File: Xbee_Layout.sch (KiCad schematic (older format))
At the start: 7 parts

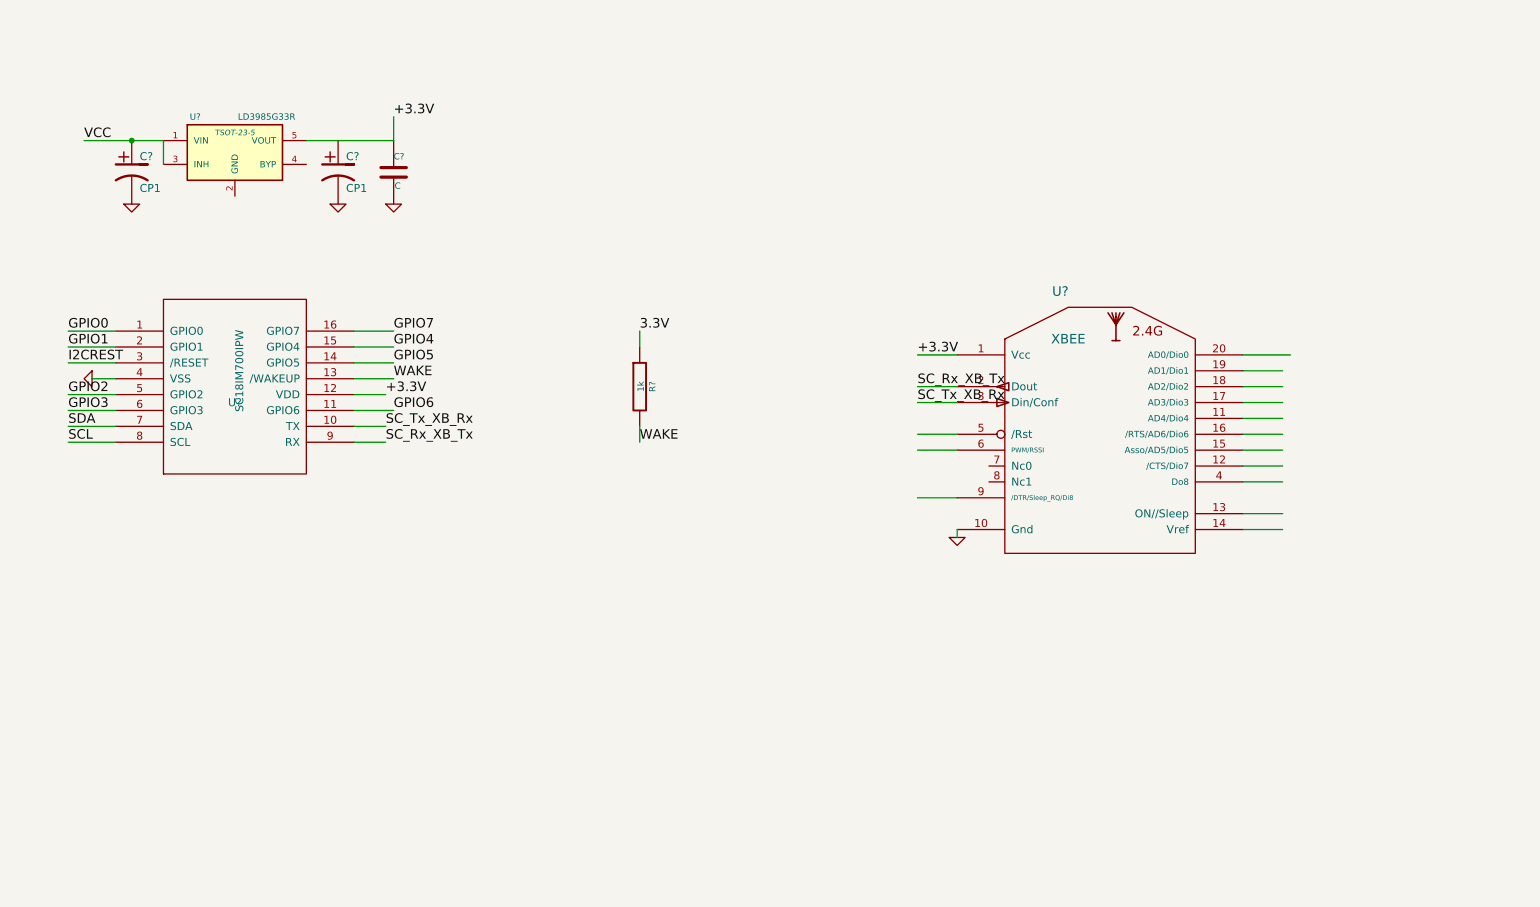
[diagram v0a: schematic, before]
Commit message: Added connectors and Jumpers
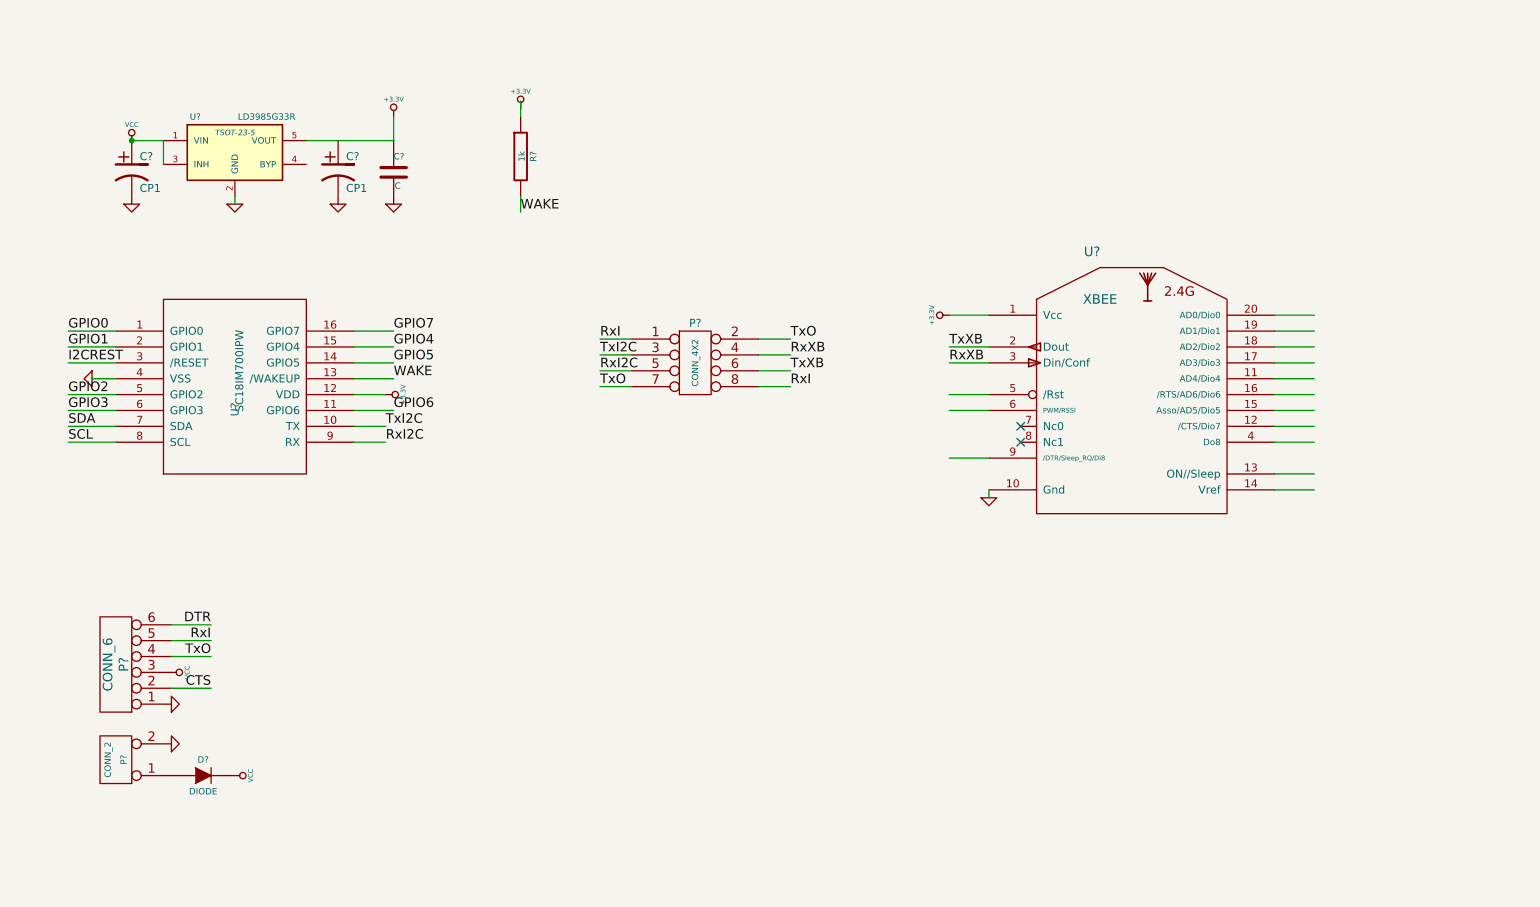
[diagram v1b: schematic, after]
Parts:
- added D?: DIODE, ~, symbol DIODE
- added P?: CONN_4X2, symbol CONN_4X2
- added P?: CONN_6, symbol CONN_6
- added P?: CONN_2, symbol CONN_2
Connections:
- net labels added: CTS, DTR, RxI, RxI2C, RxXB, TxI2C, TxO, TxXB
- net labels removed: 3.3V, SC_Rx_XB_Tx, SC_Tx_XB_Rx
- wire segments 40 -> 53
- no-connect marks 0 -> 2
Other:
- moved on the sheet: R?, U?

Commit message: I  dont kow
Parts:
- removed U?: SC18IM700IPW, TSSOP16, symbol SC18IM700IPW
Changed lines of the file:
@@
 LIBS:contrib
 LIBS:valves
+LIBS:SC18700IPW
 LIBS:Xbee_Layout-cache
 EELAYER 27 0
@@
 Sheet 1 1
 Title "noname.sch"
-Date "11 aug 2014"
+Date "12 aug 2014"
 Rev ""
 Comp ""
@@
 $EndDescr
 $Comp
-L SC18IM700IPW U?
-U 1 1 53E71C01
-P 2500 3150
-F 0 "U?" V 2500 3050 50  0000 R CNN
-F 1 "SC18IM700IPW" V 2500 3250 50  0000 C TNN
-F 2 "TSSOP16" H 2500 3150 50  0001 C CNN
-F 3 "DOCUMENTATION" H 2500 3150 50  0001 C CNN
-	1    2500 3150
-	1    0    0    -1
-$EndComp
-$Comp
 L XBEE U?

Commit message: Fixing lib still
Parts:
- removed U?: XBEE, symbol XBEE
- added U?: XBEE, symbol XBEE
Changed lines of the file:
@@
 LIBS:contrib
 LIBS:valves
-LIBS:SC18700IPW
+LIBS:sc18im700ipw
+LIBS:modules_droids
 LIBS:Xbee_Layout-cache
 EELAYER 27 0
@@
 Comment4 ""
 $EndDescr
-$Comp
-L XBEE U?
-U 1 1 53E7200D
-P 8150 3400
-F 0 "U?" H 7900 4500 60  0000 C CNN
-F 1 "XBEE" H 7950 4200 60  0000 C CNN
-F 2 "" H 8150 3400 60  0000 C CNN
-F 3 "" H 8150 3400 60  0000 C CNN
-	1    8150 3400
-	1    0    0    -1
-$EndComp
 $Comp
 L GND #PWR?
@@
 	1    0    0    -1
 $EndComp
+$Comp
+L XBEE U?
+U 1 1 53EA5E0D
+P 8150 3400
+F 0 "U?" H 7900 4500 60  0000 C CNN
+F 1 "XBEE" H 7950 4200 60  0000 C CNN
+F 2 "" H 8150 3400 60  0000 C CNN
+F 3 "" H 8150 3400 60  0000 C CNN
+	1    8150 3400
+	1    0    0    -1
+$EndComp

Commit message: Fixed everything i hope
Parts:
- added U?: SC18IM700IPW, TSSOP-16, symbol SC18IM700IPW
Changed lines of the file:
@@
 LIBS:contrib
 LIBS:valves
-LIBS:sc18im700ipw
 LIBS:modules_droids
 LIBS:Xbee_Layout-cache
@@
 	1    0    0    -1
 $EndComp
+$Comp
+L SC18IM700IPW U?
+U 1 1 53EA6645
+P 2500 3150
+F 0 "U?" H 2150 3750 50  0000 C CNN
+F 1 "SC18IM700IPW" H 2500 3600 50  0000 C CNN
+F 2 "TSSOP-16" H 2750 2550 50  0001 C CNN
+F 3 "DOCUMENTATION" V 2500 3150 50  0001 C CNN
+	1    2500 3150
+	1    0    0    -1
+$EndComp

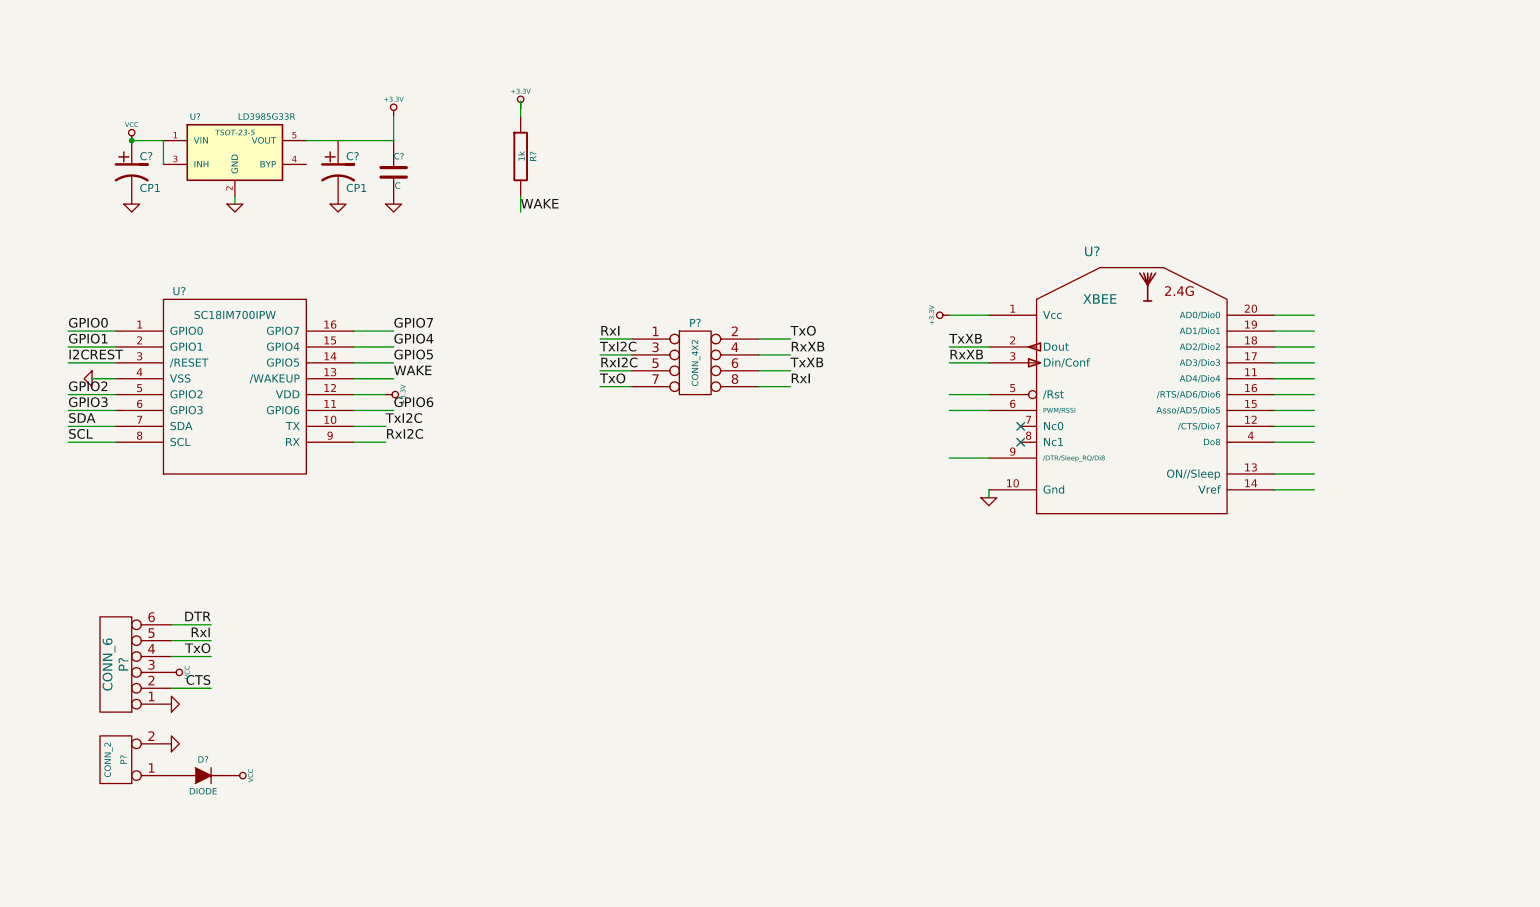
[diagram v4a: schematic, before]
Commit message: LEDs
Added power LED and rx tx indicating LEDs between the I2C module and the
XBee
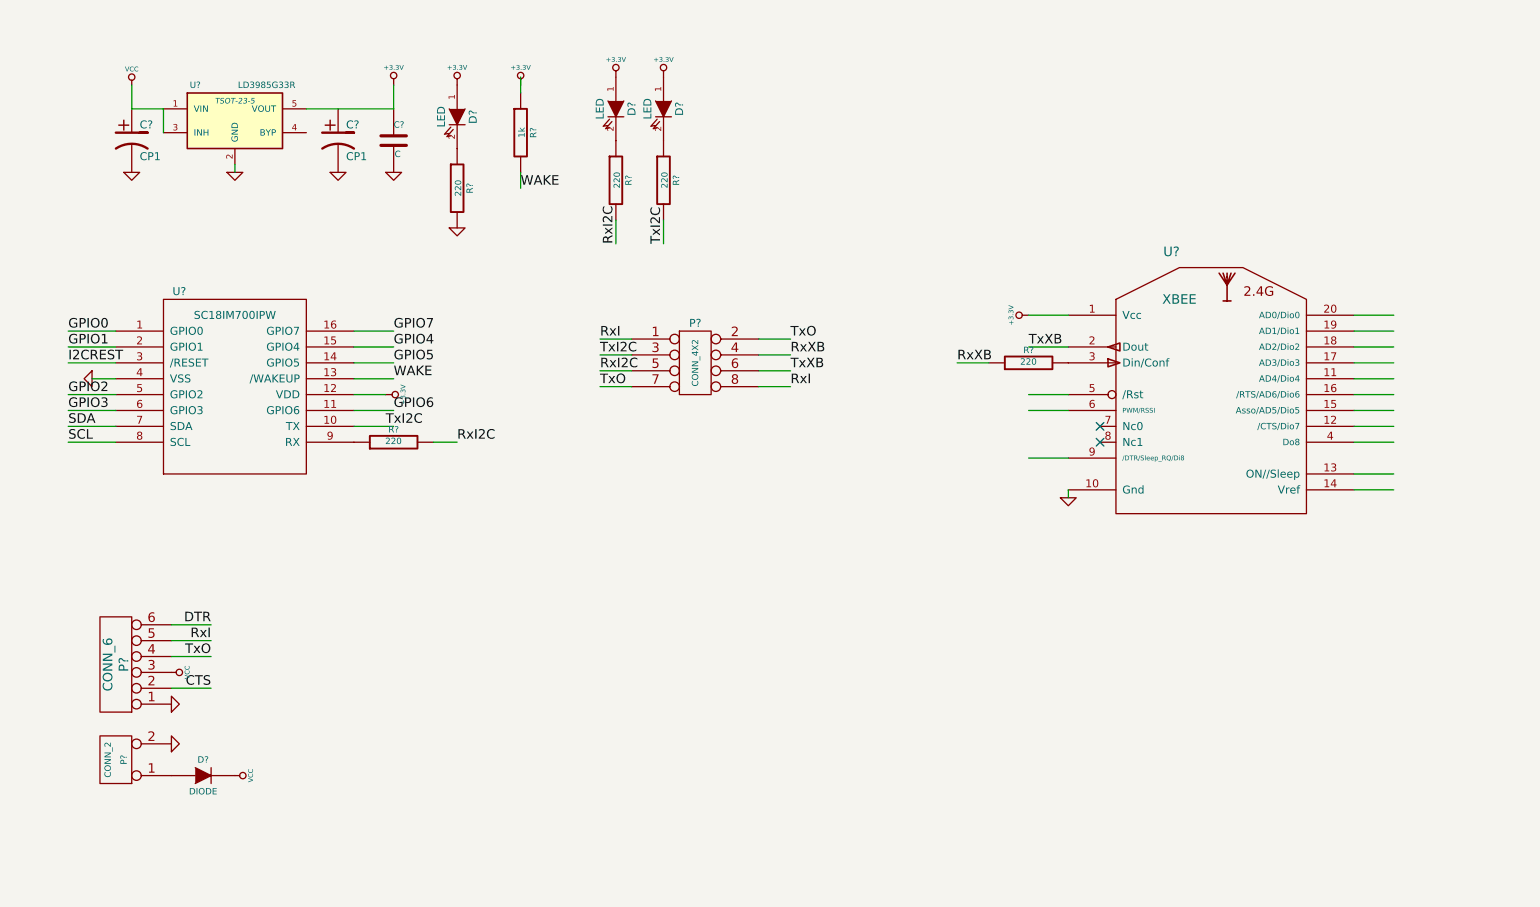
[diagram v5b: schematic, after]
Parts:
- added D? (x3): LED, ~, symbol LED
- added R? (x5): 220, ~, symbol R
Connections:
- wire segments 53 -> 56
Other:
- moved on the sheet: C?, R?, U?

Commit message: Reorganized stuff
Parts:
- added C?: C, ~, symbol C
- added D?: LED, ~, symbol LED
- added GS? (x2): GS2, ~, symbol GS2
- added R? (x2): 1k, ~, symbol R
- added R? (x2): DNP, ~, symbol R
- added R?: 220, ~, symbol R
- P?: value CONN_6 -> FTDI Breakout
- P?: value CONN_2 -> LIPO
- R? (x2): value 220 -> 30
- gave numbers to parts that had none: 2
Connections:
- net labels added: /CTS/DIO7, /RST, /RTS/DIO6, AD0/DIO0, AD1/DIO1, AD2/DIO2, AD3/DIO3, AD4/DIO4, AD5/DIO5, DIO8, ON//SLEEP, RSSI, Vref
- wire segments 56 -> 64
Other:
- note added: "Set Vref"
- moved on the sheet: D?, P?, R?, U?

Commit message: Almost finished
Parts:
- added C2: 10nF, SM0603_Capa, symbol C
- added C5: 1uF, SM0603_Capa, symbol C
- added GS1, GS4, GS5: GS2, GS2, symbol GS2
- added P1, P2: CONN_12, SIL-12, symbol CONN_12
- added P6: /RST, 1pin, symbol TST
- added P7: Vref, 1pin, symbol TST
- added Q1, Q2: BSS138, SOT-23, symbol BSS138
- added R10, R11, R12, R13: 10k, SM0603_Resistor, symbol R
- added SW1: SW_PUSH, SW_PUSH, symbol SW_PUSH
- C1, C3: renamed from C?; value CP1 -> 10uF; footprint ~ -> SM1206
- C4, C6: renamed from C?; value C -> 1uF; footprint ~ -> SM0603_Capa
- D1: renamed from D?; footprint ~ -> LED-0603
- D2: renamed from D?; footprint ~ -> SM0603
- GS2, GS3: renamed from GS?; footprint ~ -> GS2
- Green1, Green2: renamed from Green; footprint ~ -> LED-0603
- P3: renamed from P?; footprint (none) -> pin_array_4x2; Manufacturer (none) -> Molex; Maufacturer Number (none) -> 0901310764
- P4: renamed from P?; Manufacturer (none) -> 4UCON; Manufacturer Number (none) -> Unknown; Vendor (none) -> Sparkfun; Vendor Number (none) -> PRT-08612
- P5: renamed from P?; Manufacturer (none) -> 4UCON; Manufacturer Number (none) -> Unknown; Vendor (none) -> Sparkfun; Vendor Number (none) -> PRT-09015
- R1, R14, R15, R2, R3, R4, R5, R6, R7, R8, R9: renamed from R?; footprint ~ -> SM0603_Resistor
- RED1: renamed from RED; footprint ~ -> LED-0603
- gave numbers to parts that had none: 3
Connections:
- net labels added: /CTS, /DTR, /RTS, AD0, AD1, AD2, AD3, AD4, AD5, CTSO, DO8, ON, PWM1, Tx
- net labels removed: /CTS/DIO7, /RTS/DIO6, AD0/DIO0, AD1/DIO1, AD2/DIO2, AD3/DIO3, AD4/DIO4, AD5/DIO5, DIO8, ON//SLEEP
- wire segments 64 -> 108
- no-connect marks 2 -> 1
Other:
- note added: "I2CReset"
- note added: "Level Translation"
- moved on the sheet: C6, D1, GS2, GS3, Green1, Green2, P3, R14, R15, R5, R6, R7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
